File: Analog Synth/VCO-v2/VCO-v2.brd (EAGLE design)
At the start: 100 x 100 mm, 42 parts, among them IC1 TL084P, IC2 TL084P, T1 2N3904, T2 2N3904, T3 2N3904, U1 CA3096

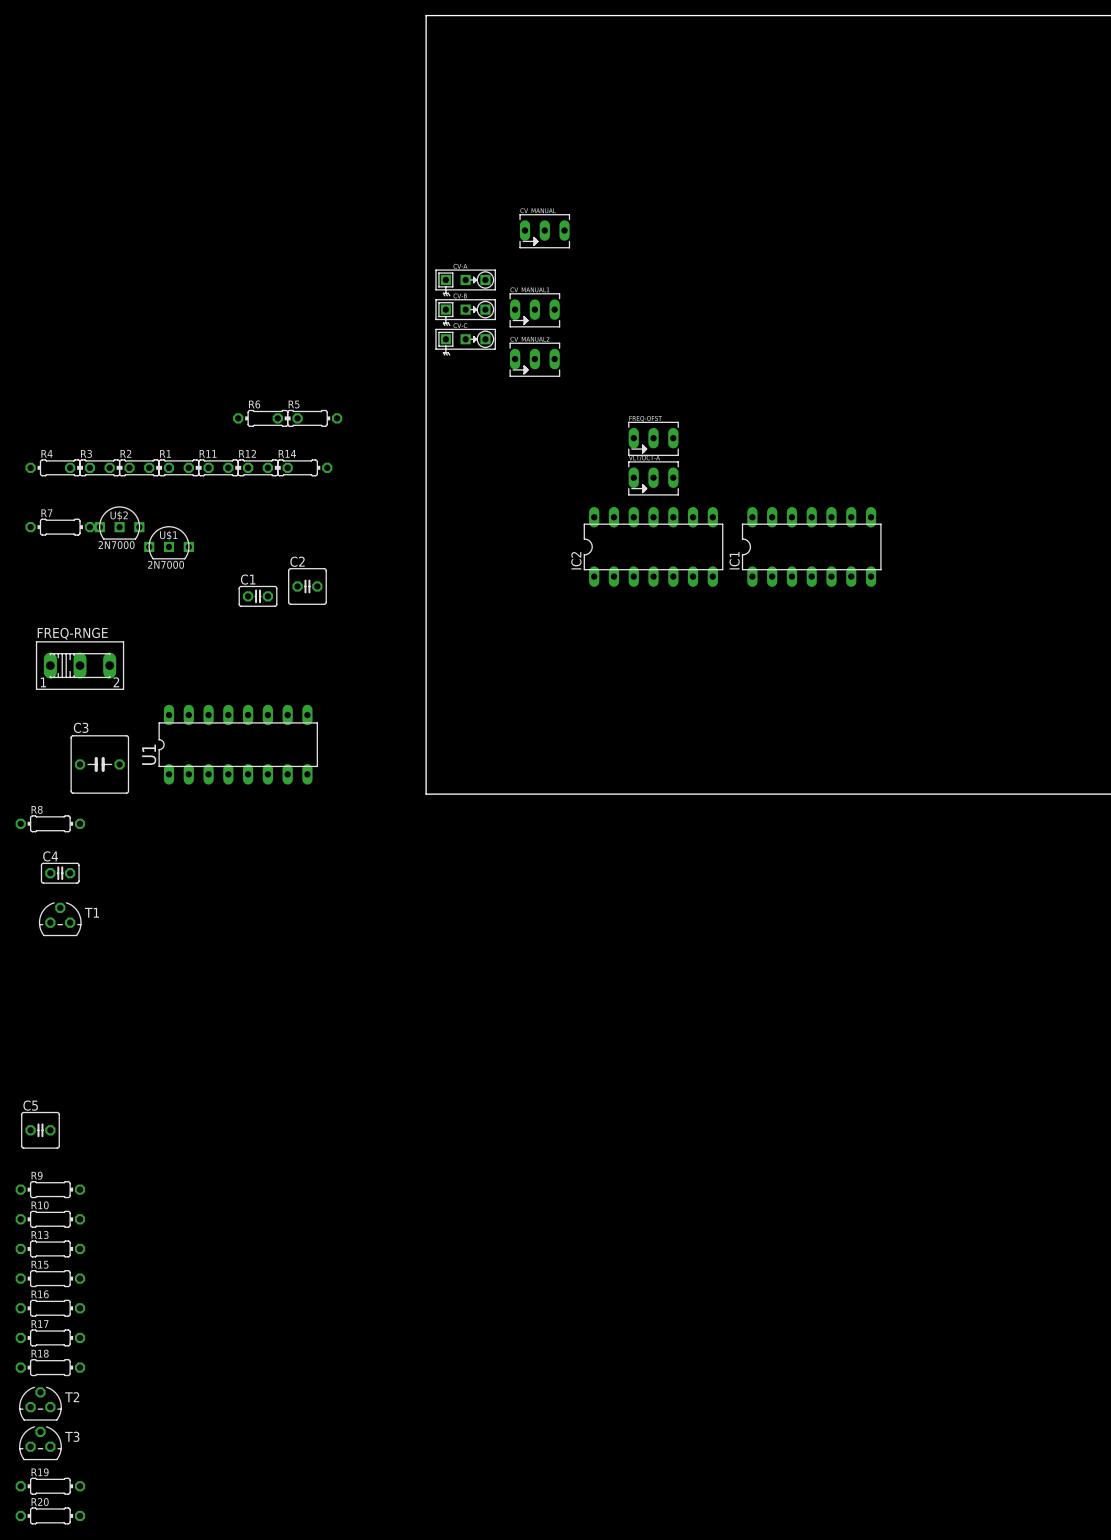
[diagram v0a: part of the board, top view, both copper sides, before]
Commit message: VCO-v2 high frequency compensation
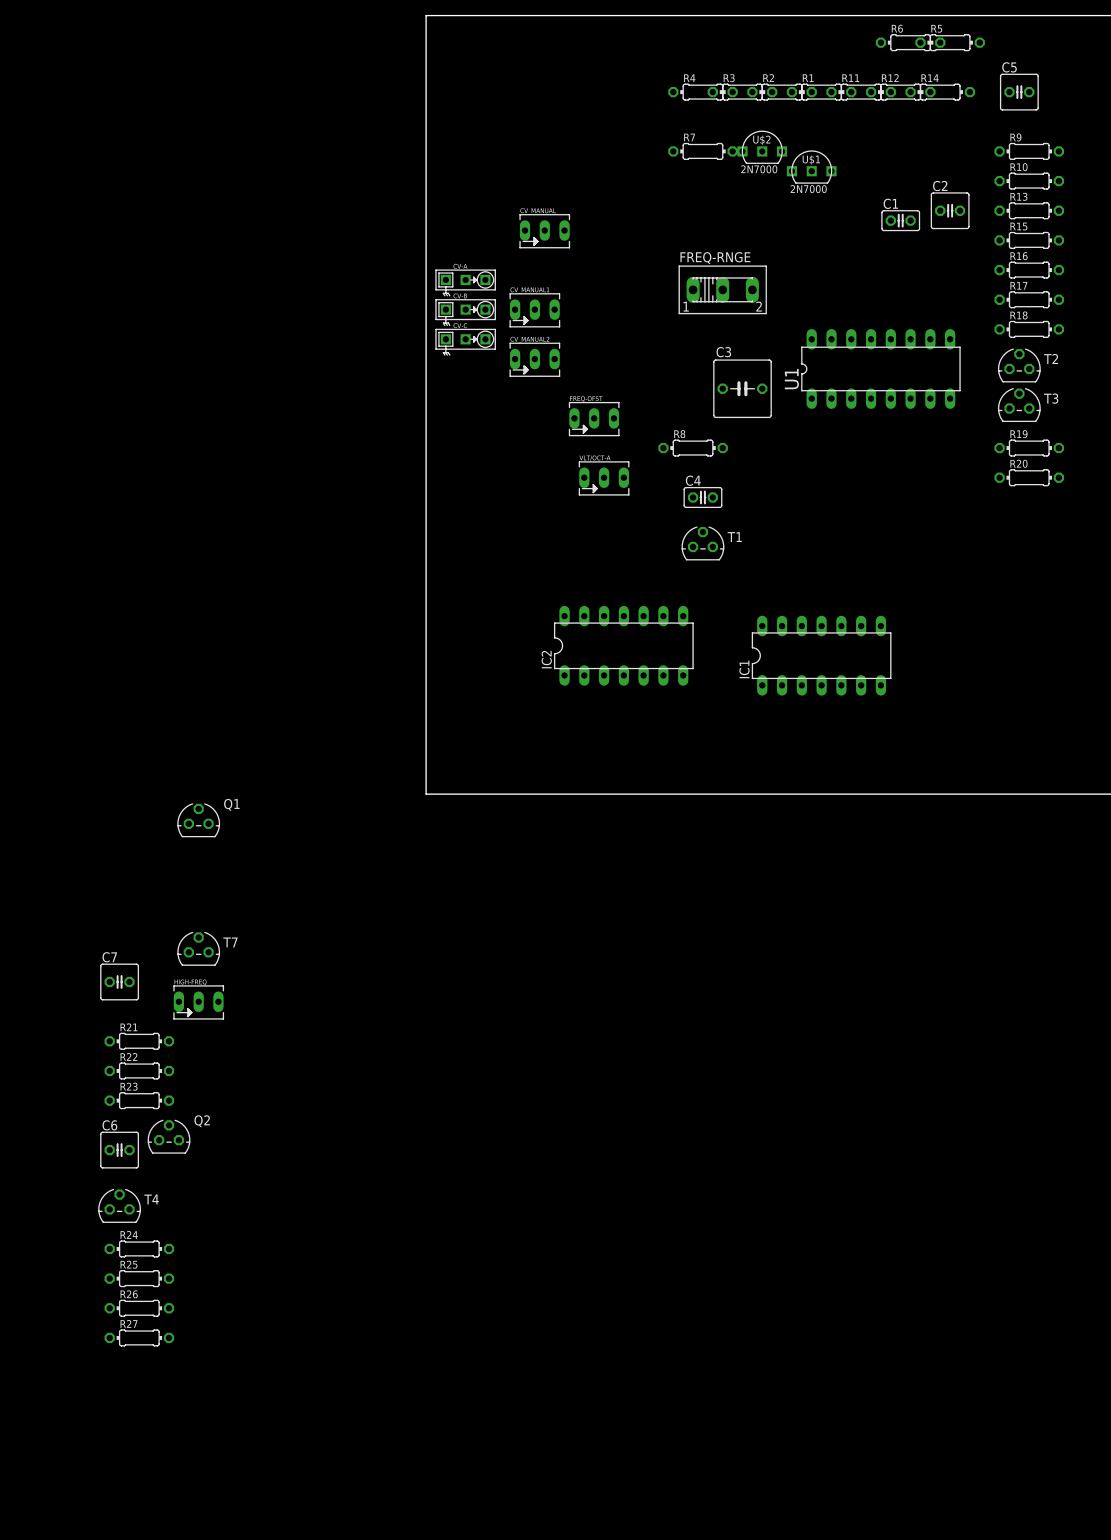
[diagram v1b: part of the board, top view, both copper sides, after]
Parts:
- added C6, C7: 300p, resistor:C025-050X050
- added HIGH-FREQ: 100k trim, pot:B64Y
- added Q1, Q2: J310, transistor-small-signal:TO92R
- added R21, R23, R24, R26: 10k, resistor:0204/7
- added R22, R25: 100k, resistor:0204/7
- added R27: 47k, resistor:0204/7
- added T4, T7: 2N3904, transistor-neu-to92:TO92
- moved C5 183.3 mm to (76.2, 90.2)
- moved R13 183.3 mm to (77.5, 74.9)
- moved R16 183.3 mm to (77.5, 67.3)
- moved R19 183.3 mm to (77.5, 44.5)
- moved T2 183.3 mm to (76.2, 54.6)
- moved T3 183.3 mm to (76.2, 49.5)
- moved R10 183.3 mm to (77.5, 78.7)
- moved R15 183.3 mm to (77.5, 71.1)
- moved R17 183.3 mm to (77.5, 63.5)
- moved R18 183.3 mm to (77.5, 59.7)
- moved R20 183.3 mm to (77.5, 40.6)
- moved R9 183.3 mm to (77.5, 82.5)
- moved C4 95.6 mm to (35.6, 38.1)
- moved FREQ-RNGE 95.6 mm to (38.1, 64.8)
- moved R11 95.6 mm to (55.9, 90.2)
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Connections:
- new net N$25: Q1.D, R21.1, R23.1
- new net N$26: C7.2, Q1.G, R22.2, T7.2
- new net N$29: Q2.D, R24.1, R26.1
- new net N$31: C6.2, Q2.G, R25.2, T4.2
- new net N$32: HIGH-FREQ.A, R23.2, R26.2
- new net N$33: HIGH-FREQ.S, R27.1
- net -5V: now also HIGH-FREQ.E, Q1.S, Q2.S, R22.1, R25.1
- net CV_SUM_POINT: now also R27.2
- net GND: now also R21.2, R24.2, T4.1, T4.3, T7.1, T7.3
- net RAMP_DOWN: now also C6.1
- net RAMP_UP: now also C7.1

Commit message: VCO-v2
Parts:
- added U$3: EURORACK-POWER, !synth_sch:EURORACK-POWER
- moved Q2 176.0 mm to (88.9, 82.5)
- moved HIGH-FREQ 155.1 mm to (90.2, 72.4)
- moved R26 149.0 mm to (92.7, 7.62)
- moved C6 149.0 mm to (90.2, 27.9)
- moved C7 149.0 mm to (90.2, 49.5)
- moved R21 149.0 mm to (92.7, 41.9)
- moved R22 149.0 mm to (92.7, 38.1)
- moved R23 149.0 mm to (92.7, 34.3)
- moved R24 149.0 mm to (92.7, 15.2)
- moved R25 149.0 mm to (92.7, 11.4)
- moved R27 149.0 mm to (92.7, 3.81)
- moved T4 149.0 mm to (90.2, 20.3)
- moved T7 147.3 mm to (90.2, 66.0)
- moved Q1 135.2 mm to (91.4, 57.1)
- moved R4 67.4 mm to (85.1, 44.5), turned to 90 degrees
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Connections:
- new net N$27: U$3.P$3, U$3.P$5, U$3.P$7
- new net N$28: U$3.P$4, U$3.P$6, U$3.P$8
- new net N$34: U$3.P$1, U$3.P$2
- new net N$35: U$3.P$10, U$3.P$9

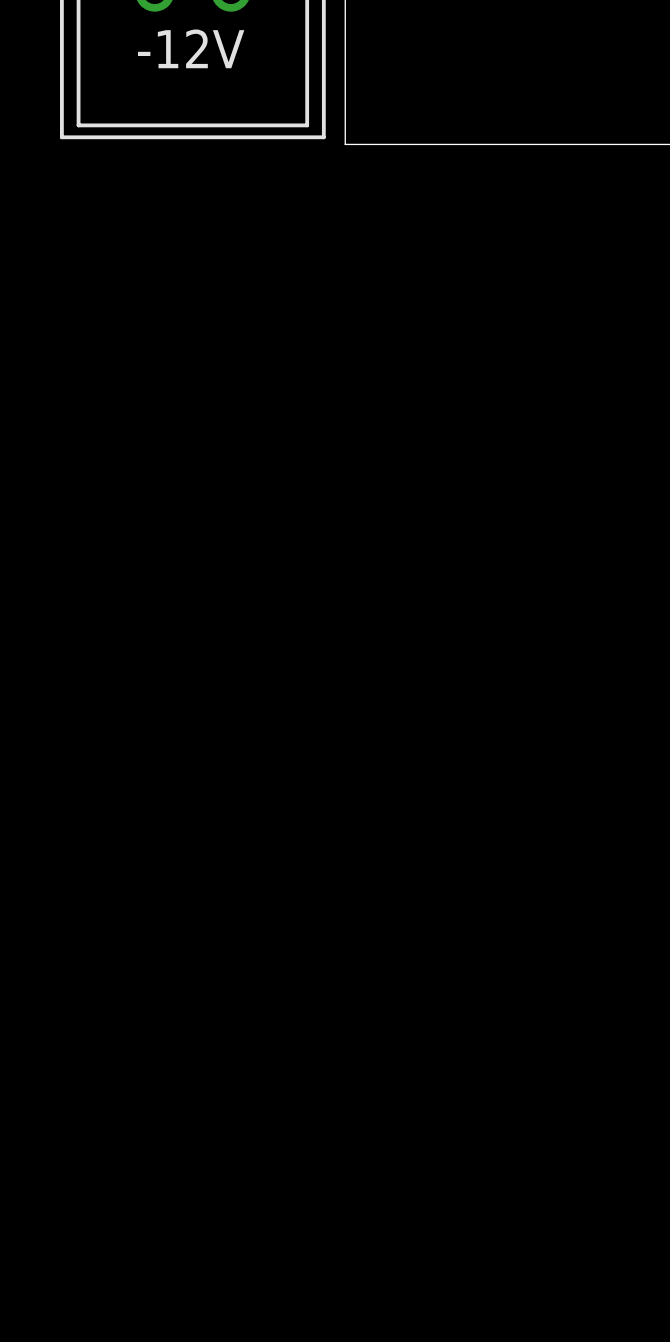
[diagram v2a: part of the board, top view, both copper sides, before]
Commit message: VCO-v2 - power supply. Also, I need to change those integration caps to be polarized types in the schematic and on the pcb...
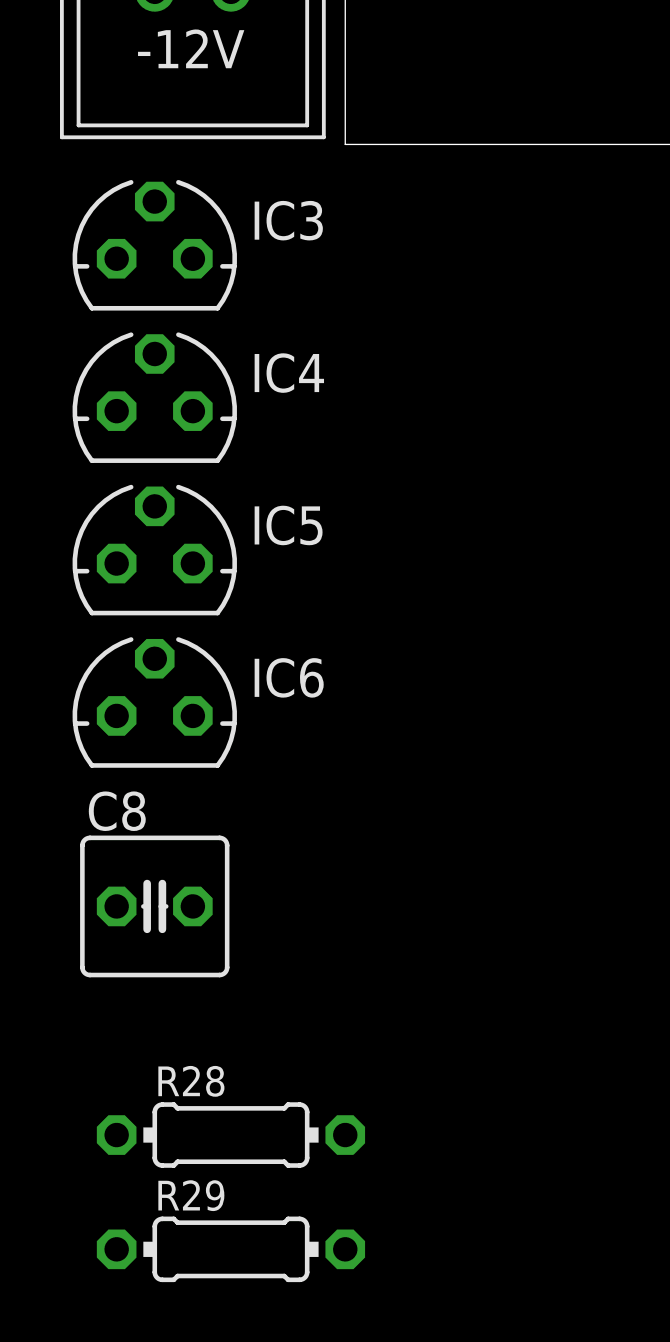
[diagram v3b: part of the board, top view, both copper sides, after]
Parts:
- added C8: 100p, resistor:C025-050X050
- added IC3: 78L09, v-reg:78LXX
- added IC4: (no value), v-reg:78LXX
- added IC5: 79L09\, v-reg:79LXX
- added IC6: (no value), v-reg:79LXX
- added R28, R29: 7.5, resistor:0204/7
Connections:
- removed net N$27: U$3.P$3, U$3.P$5, U$3.P$7
- removed net N$28: U$3.P$4, U$3.P$6, U$3.P$8
- new net +12V: IC3.IN, IC4.IN, R28.2
- net +5V: now also IC4.OUT
- net +9V: now also IC3.OUT
- net -12V: now also IC5.IN, IC6.IN, R29.1
- net -5V: now also IC6.OUT
- net -9V: now also IC5.OUT
- net GND: now also IC3.GND, IC4.GND, IC6.GND, U$3.P$3, U$3.P$4, U$3.P$5, U$3.P$6, U$3.P$7, U$3.P$8
- net N$34: now also R28.1
- net N$35: now also R29.2
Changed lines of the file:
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@@
 <element name="R27" library="resistor" package="0204/7" value="47k" x="92.71" y="3.81"/>
 <element name="U$3" library="!synth_sch" package="EURORACK-POWER" value="EURORACK-POWER" x="-5.08" y="10.16"/>
+<element name="IC3" library="v-reg" package="78LXX" value="78L09" x="-6.35" y="-3.81"/>
+<element name="IC4" library="v-reg" package="78LXX" value="" x="-6.35" y="-8.89"/>
+<element name="IC5" library="v-reg" package="79LXX" value="79L09\" x="-6.35" y="-13.97"/>
+<element name="IC6" library="v-reg" package="79LXX" value="" x="-6.35" y="-19.05"/>
+<element name="C8" library="resistor" package="C025-050X050" value="100p" x="-6.35" y="-25.4"/>
+<element name="R28" library="resistor" package="0204/7" value="7.5" x="-3.81" y="-33.02"/>
+<element name="R29" library="resistor" package="0204/7" value="7.5" x="-3.81" y="-36.83"/>
 </elements>
 <signals>
@@
 <contactref element="T4" pad="1"/>
 <contactref element="T4" pad="3"/>
+<contactref element="IC3" pad="GND"/>
+<contactref element="U$3" pad="P$3"/>
+<contactref element="U$3" pad="P$5"/>
+<contactref element="U$3" pad="P$7"/>
+<contactref element="U$3" pad="P$8"/>
+<contactref element="U$3" pad="P$6"/>
+<contactref element="U$3" pad="P$4"/>
+<contactref element="IC6" pad="GND"/>
+<contactref element="IC4" pad="GND"/>
 <wire x1="88.9" y1="66.04" x2="91.44" y2="66.04" width="0" layer="19" extent="1-1"/>
 <wire x1="96.52" y1="41.91" x2="91.44" y2="66.04" width="0" layer="19" extent="1-1"/>
@@
 <wire x1="88.9" y1="20.32" x2="91.44" y2="20.32" width="0" layer="19" extent="1-1"/>
 <wire x1="96.52" y1="15.24" x2="91.44" y2="20.32" width="0" layer="19" extent="1-1"/>
-<wire x1="22.86" y1="7.62" x2="88.9" y2="20.32" width="0" layer="19" extent="1-1"/>
 <wire x1="30.48" y1="87.63" x2="88.9" y2="66.04" width="0" layer="19" extent="1-1"/>
 <wire x1="21.59" y1="83.82" x2="30.48" y2="87.63" width="0" layer="19" extent="1-1"/>
@@
 <wire x1="15.24" y1="92.71" x2="17.78" y2="92.71" width="0" layer="19" extent="1-1"/>
 <wire x1="15.24" y1="96.52" x2="15.24" y2="92.71" width="0" layer="19" extent="1-1"/>
+<wire x1="22.86" y1="7.62" x2="88.9" y2="20.32" width="0" layer="19" extent="1-1"/>
+<wire x1="-3.81" y1="7.62" x2="22.86" y2="7.62" width="0" layer="19" extent="1-1"/>
+<wire x1="-3.81" y1="10.16" x2="-3.81" y2="7.62" width="0" layer="19" extent="1-1"/>
+<wire x1="-3.81" y1="12.7" x2="-3.81" y2="10.16" width="0" layer="19" extent="1-1"/>
+<wire x1="-6.35" y1="12.7" x2="-3.81" y2="12.7" width="0" layer="19" extent="1-1"/>
+<wire x1="-6.35" y1="10.16" x2="-3.81" y2="10.16" width="0" layer="19" extent="1-1"/>
+<wire x1="-6.35" y1="7.62" x2="-3.81" y2="7.62" width="0" layer="19" extent="1-1"/>
+<wire x1="-6.35" y1="-1.905" x2="-6.35" y2="7.62" width="0" layer="19" extent="1-1"/>
+<wire x1="-6.35" y1="-6.985" x2="-6.35" y2="-1.905" width="0" layer="19" extent="1-1"/>
+<wire x1="-7.62" y1="-19.05" x2="-6.35" y2="-6.985" width="0" layer="19" extent="1-1"/>
 </signal>
 <signal name="N$11">
@@
 <contactref element="U1" pad="13"/>
 <contactref element="R7" pad="2"/>
+<contactref element="IC4" pad="OUT"/>
 <wire x1="31.75" y1="95.25" x2="41.91" y2="88.9" width="0" layer="19" extent="1-1"/>
 <wire x1="64.77" y1="15.24" x2="41.91" y2="88.9" width="0" layer="19" extent="1-1"/>
 <wire x1="72.39" y1="15.24" x2="64.77" y2="15.24" width="0" layer="19" extent="1-1"/>
+<wire x1="-7.62" y1="-8.89" x2="64.77" y2="15.24" width="0" layer="19" extent="1-1"/>
 </signal>
 <signal name="-5V">
@@
 <contactref element="R25" pad="1"/>
 <contactref element="HIGH-FREQ" pad="E"/>
+<contactref element="IC6" pad="OUT"/>
 <wire x1="87.63" y1="72.39" x2="88.9" y2="84.455" width="0" layer="19" extent="1-1"/>
 <wire x1="85.09" y1="71.12" x2="87.63" y2="72.39" width="0" layer="19" extent="1-1"/>
@@
 <wire x1="73.66" y1="36.83" x2="71.12" y2="44.45" width="0" layer="19" extent="1-1"/>
 <wire x1="88.9" y1="38.1" x2="73.66" y2="36.83" width="0" layer="19" extent="1-1"/>
-<wire x1="67.31" y1="7.62" x2="73.66" y2="36.83" width="0" layer="19" extent="1-1"/>
-<wire x1="74.93" y1="7.62" x2="67.31" y2="7.62" width="0" layer="19" extent="1-1"/>
-<wire x1="88.9" y1="11.43" x2="74.93" y2="7.62" width="0" layer="19" extent="1-1"/>
+<wire x1="88.9" y1="11.43" x2="88.9" y2="38.1" width="0" layer="19" extent="1-1"/>
+<wire x1="74.93" y1="7.62" x2="88.9" y2="11.43" width="0" layer="19" extent="1-1"/>
+<wire x1="67.31" y1="7.62" x2="74.93" y2="7.62" width="0" layer="19" extent="1-1"/>
 <wire x1="26.67" y1="95.25" x2="67.31" y2="82.55" width="0" layer="19" extent="1-1"/>
 <wire x1="5.08" y1="82.55" x2="26.67" y2="95.25" width="0" layer="19" extent="1-1"/>
+<wire x1="-5.08" y1="-19.05" x2="67.31" y2="7.62" width="0" layer="19" extent="1-1"/>
 </signal>
 <signal name="NPN_CV">
@@
 <signal name="-12V">
 <contactref element="U1" pad="16"/>
+<contactref element="R29" pad="1"/>
+<contactref element="IC5" pad="IN"/>
+<contactref element="IC6" pad="IN"/>
+<wire x1="-6.35" y1="-12.065" x2="57.15" y2="15.24" width="0" layer="19" extent="1-1"/>
+<wire x1="-6.35" y1="-17.145" x2="-6.35" y2="-12.065" width="0" layer="19" extent="1-1"/>
+<wire x1="-7.62" y1="-36.83" x2="-6.35" y2="-17.145" width="0" layer="19" extent="1-1"/>
 </signal>
 <signal name="TRIANGLE-RAW">
@@
 <contactref element="R10" pad="1"/>
 <contactref element="R9" pad="1"/>
+<contactref element="IC5" pad="OUT"/>
 <wire x1="73.66" y1="78.74" x2="73.66" y2="82.55" width="0" layer="19" extent="1-1"/>
+<wire x1="-5.08" y1="-13.97" x2="73.66" y2="78.74" width="0" layer="19" extent="1-1"/>
 </signal>
 <signal name="N$30">
@@
 <contactref element="R17" pad="1"/>
 <contactref element="R19" pad="2"/>
+<contactref element="IC3" pad="OUT"/>
 <wire x1="73.66" y1="63.5" x2="81.28" y2="67.31" width="0" layer="19" extent="1-1"/>
 <wire x1="81.28" y1="44.45" x2="73.66" y2="63.5" width="0" layer="19" extent="1-1"/>
+<wire x1="-7.62" y1="-3.81" x2="81.28" y2="44.45" width="0" layer="19" extent="1-1"/>
 </signal>
 <signal name="N$25">
@@
 <wire x1="88.9" y1="3.81" x2="90.17" y2="72.39" width="0" layer="19" extent="1-1"/>
 </signal>
-<signal name="N$27">
-<contactref element="U$3" pad="P$3"/>
-<contactref element="U$3" pad="P$5"/>
-<contactref element="U$3" pad="P$7"/>
-<wire x1="-6.35" y1="10.16" x2="-6.35" y2="12.7" width="0" layer="19" extent="1-1"/>
-<wire x1="-6.35" y1="7.62" x2="-6.35" y2="10.16" width="0" layer="19" extent="1-1"/>
-</signal>
-<signal name="N$28">
-<contactref element="U$3" pad="P$8"/>
-<contactref element="U$3" pad="P$6"/>
-<contactref element="U$3" pad="P$4"/>
-<wire x1="-3.81" y1="10.16" x2="-3.81" y2="12.7" width="0" layer="19" extent="1-1"/>
-<wire x1="-3.81" y1="7.62" x2="-3.81" y2="10.16" width="0" layer="19" extent="1-1"/>
-</signal>
 <signal name="N$34">
 <contactref element="U$3" pad="P$1"/>
 <contactref element="U$3" pad="P$2"/>
-<wire x1="-6.35" y1="15.24" x2="-3.81" y2="15.24" width="0" layer="19" extent="1-1"/>
+<contactref element="R28" pad="1"/>
+<wire x1="-6.35" y1="15.24" x2="-7.62" y2="-33.02" width="0" layer="19" extent="1-1"/>
+<wire x1="-3.81" y1="15.24" x2="-6.35" y2="15.24" width="0" layer="19" extent="1-1"/>
 </signal>
 <signal name="N$35">
 <contactref element="U$3" pad="P$9"/>
 <contactref element="U$3" pad="P$10"/>
+<contactref element="R29" pad="2"/>
+<wire x1="-3.81" y1="5.08" x2="0" y2="-36.83" width="0" layer="19" extent="1-1"/>
 <wire x1="-6.35" y1="5.08" x2="-3.81" y2="5.08" width="0" layer="19" extent="1-1"/>
 </signal>
+<signal name="+12V">
+<contactref element="R28" pad="2"/>
+<contactref element="IC3" pad="IN"/>
+<contactref element="IC4" pad="IN"/>
+<wire x1="-5.08" y1="-8.89" x2="0" y2="-33.02" width="0" layer="19" extent="1-1"/>
+<wire x1="-5.08" y1="-3.81" x2="-5.08" y2="-8.89" width="0" layer="19" extent="1-1"/>
+</signal>
 </signals>
